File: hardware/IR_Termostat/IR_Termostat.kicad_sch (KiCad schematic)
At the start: 16 parts, among them J1 USB_C_Receptacle_PowerOnly_6P, Q1 PMOS, U1 TP4056-42-ESOP8, U2 XC6206P-3.3V

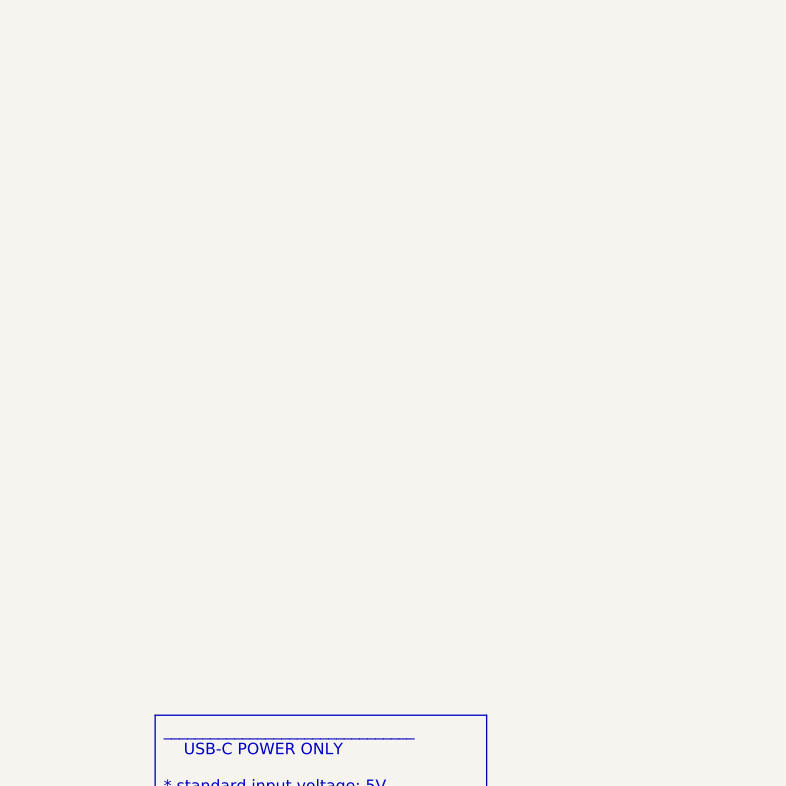
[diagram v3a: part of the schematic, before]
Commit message: feat: Battery protection circuit implemented
Added a protection resiable IC for: Over and Under charge, short, inverse polarity
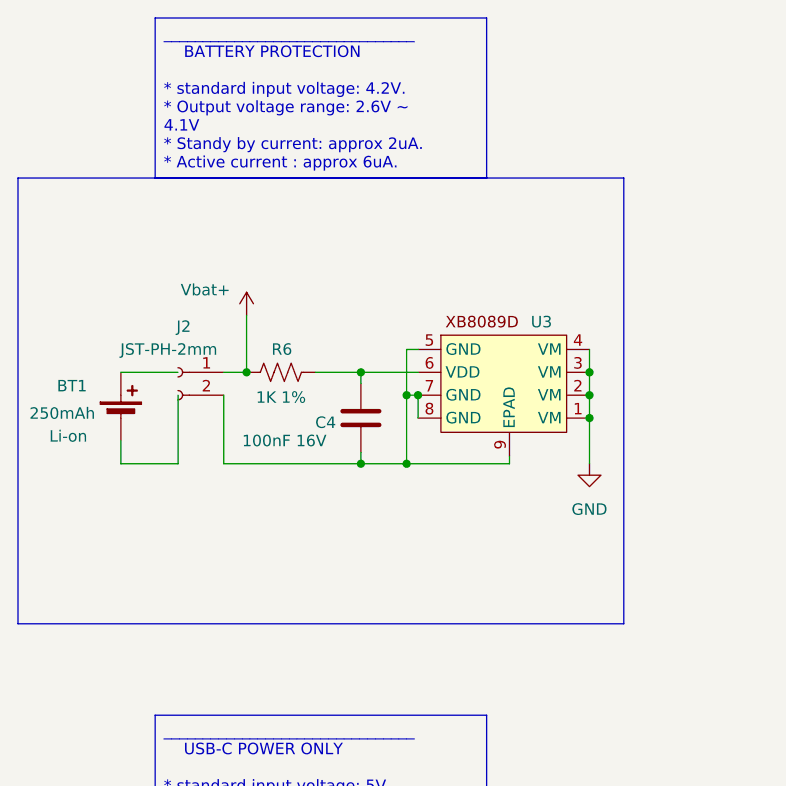
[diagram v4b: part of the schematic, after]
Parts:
- added BT1: 250mAh, symbol Device:Battery_Cell
- added C4: 100nF 16V, Capacitor_SMD:C_0805_2012Metric_Pad1.18x1.45mm_HandSolder, symbol Device:C
- added J2: JST-PH-2mm, Connector_JST:JST_PH_S2B-PH-K_1x02_P2.00mm_Horizontal, symbol Connector:Conn_01x02_Socket
- added R6: 1K 1%, Resistor_SMD:R_0805_2012Metric_Pad1.20x1.40mm_HandSolder, symbol Device:R_US
- added U3: ~, symbol Custom_lib:XB8089D
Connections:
- net GND: now also U3.1 (VM), U3.2 (VM), U3.3 (VM), U3.4 (VM)
- net Vbat+: now also J2.1 (Pin_1), R6.1
- new net: C4.1, R6.2, U3.6 (VDD)
- new net: C4.2, J2.2 (Pin_2), U3.5 (GND), U3.7 (GND), U3.8 (GND), U3.9 (EPAD)

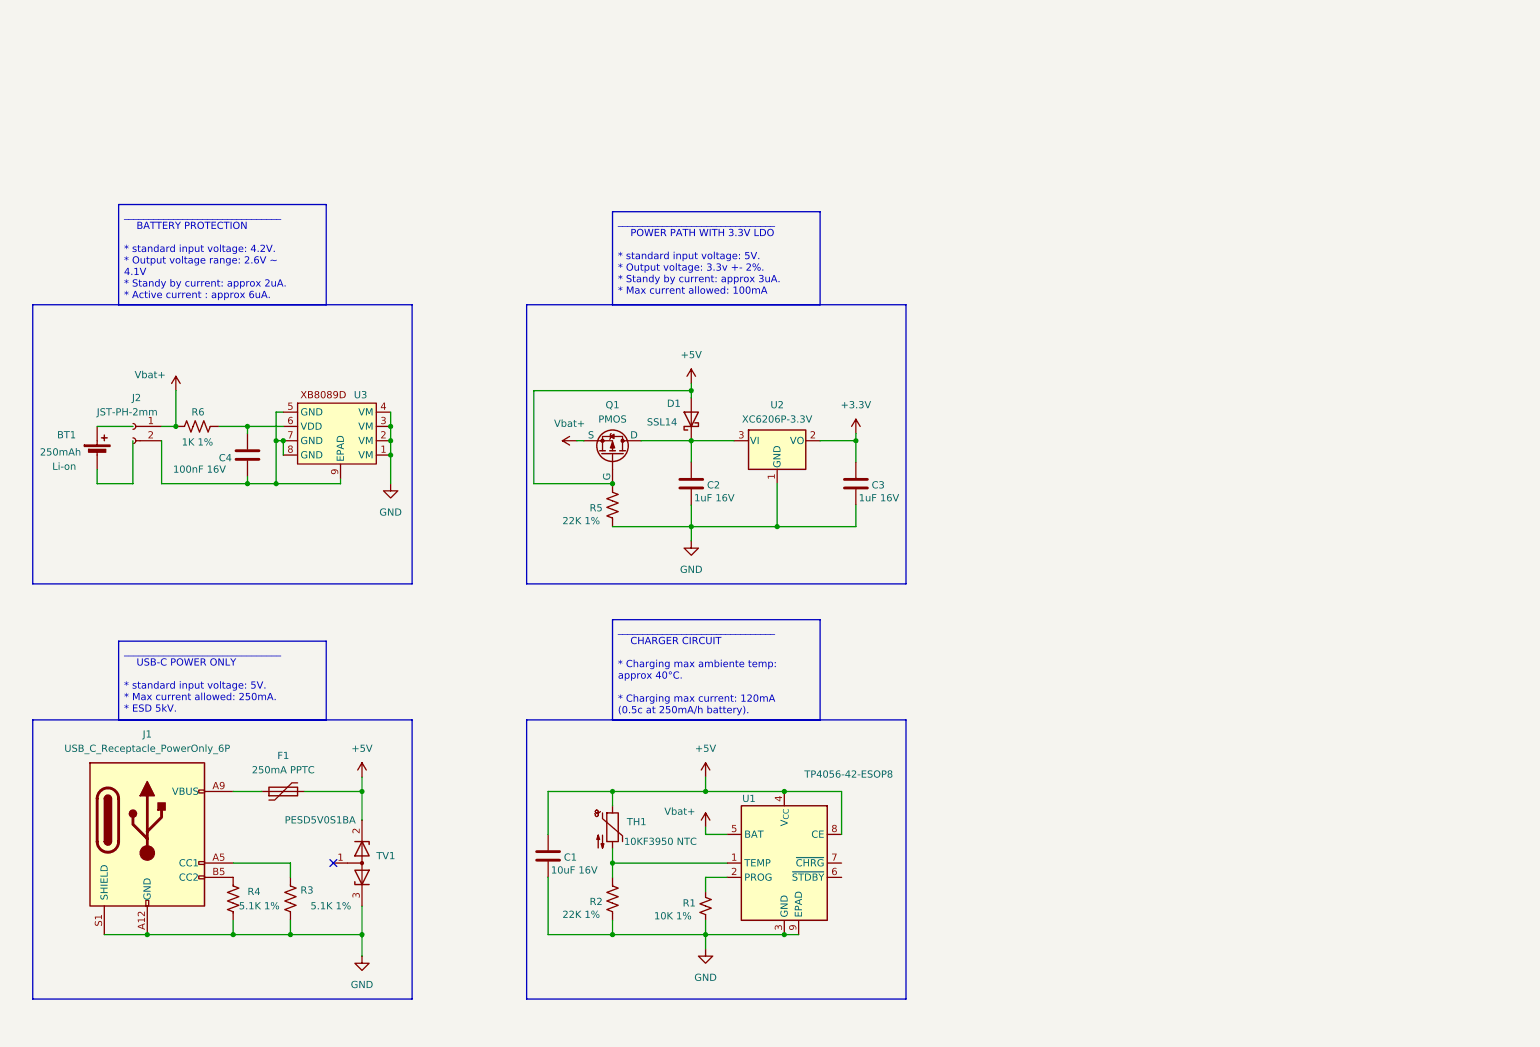
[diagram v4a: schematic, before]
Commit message: feat: pullup resistor to charge IC I/Os
 Also redesingned the sch. for better visual
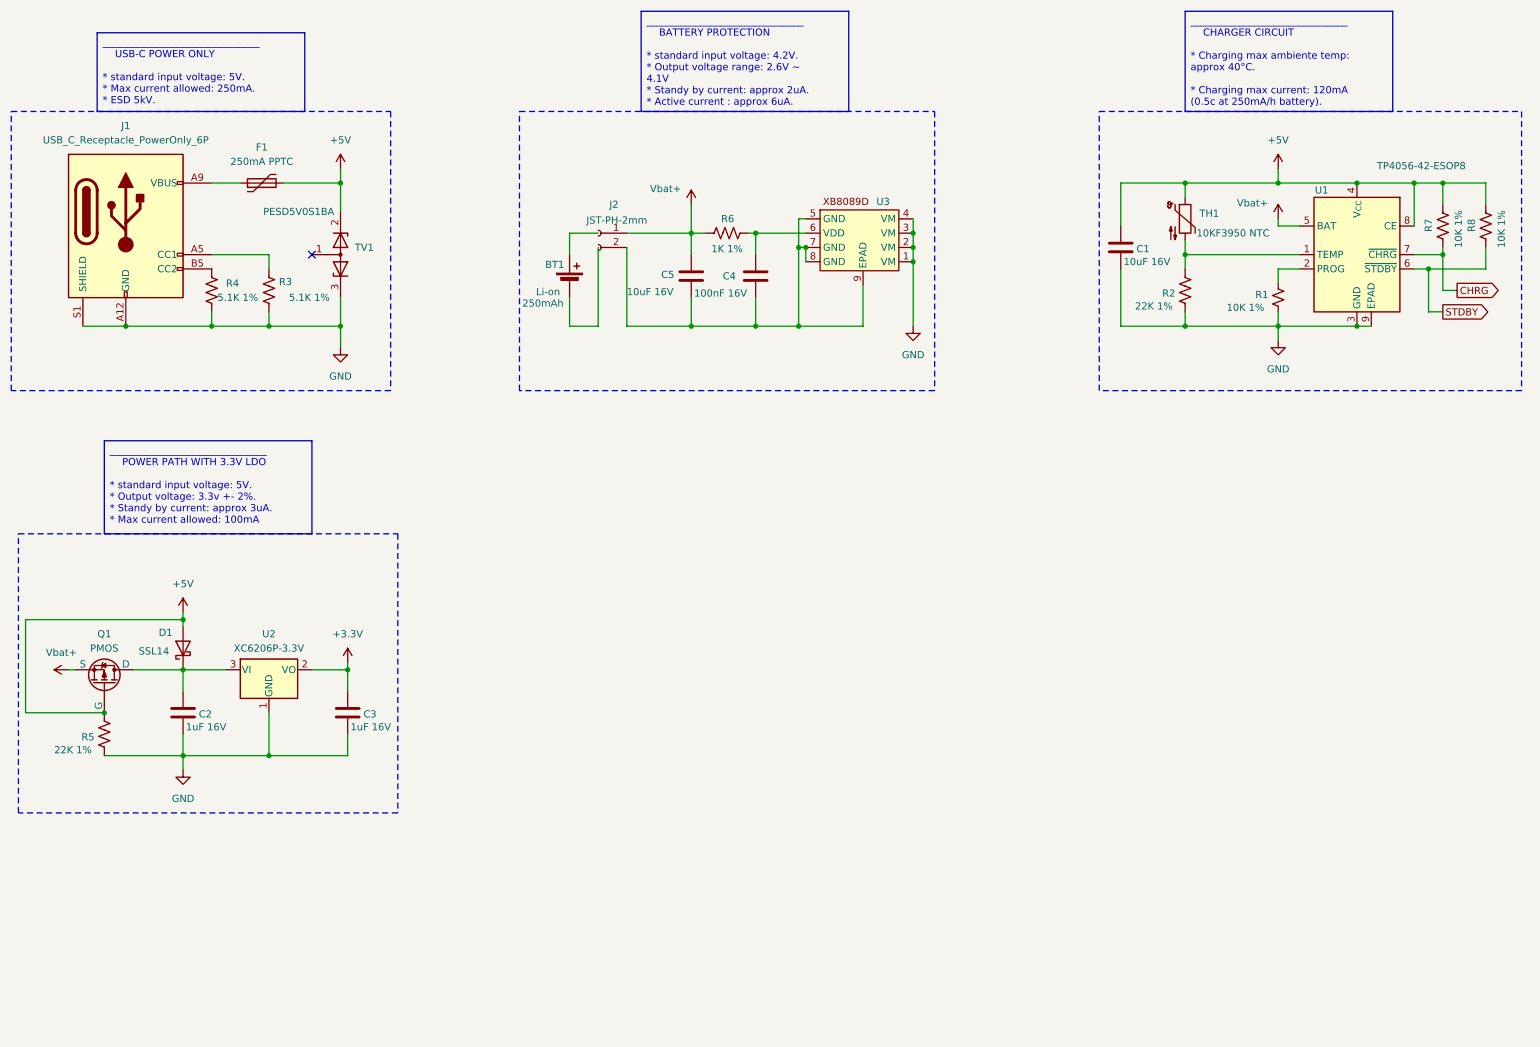
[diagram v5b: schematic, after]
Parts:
- added C5: 10uF 16V, Capacitor_SMD:C_0805_2012Metric_Pad1.18x1.45mm_HandSolder, symbol Device:C
- added R7, R8: 10K 1%, Resistor_SMD:R_0805_2012Metric_Pad1.20x1.40mm_HandSolder, symbol Device:R_US
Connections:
- net +5V: now also R7.2, R8.2
- net Vbat+: now also C5.1
- net at C4.2, J2.2 (Pin_2), U3.5 (GND)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: now also C5.2
- net STDBY: now reaches U1.6 (~{STDBY})
- net STDBY: now also R8.1
- net CHRG: now reaches U1.7 (~{CHRG})
- net CHRG: now also R7.1
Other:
- moved on the sheet: BT1, C1, C2, C3, C4, D1, F1, J1, J2, Q1, R1, R2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

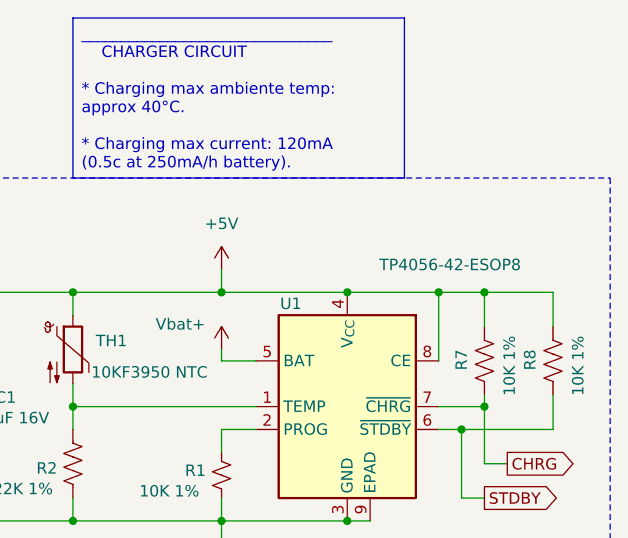
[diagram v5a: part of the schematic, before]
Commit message: Fix: Switched Pullup resistors source from TP4056
Before, the resistors responsable for the pullup of the CHRGD and STDBY pins from the charger IC are connect on 5V line, now they are on 3.3V power supply from LDO.
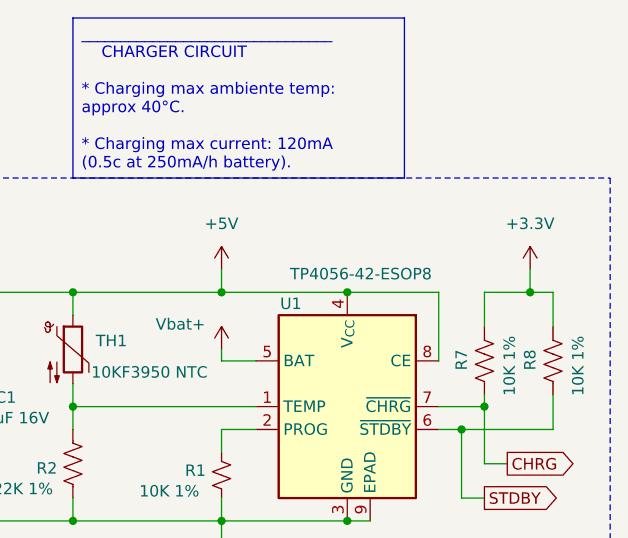
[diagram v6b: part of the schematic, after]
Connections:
- net +3.3V: now also R7.2, R8.2
- net +5V: no longer R7.2, R8.2
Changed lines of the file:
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@@
-	)
-	(junction
-		(at 267.97 44.45)
-		(diameter 0)
-		(color 0 0 0 0)
 	)
 	(junction
@@
 	)
 	(junction
-		(at 262.89 44.45)
-		(diameter 0)
-		(color 0 0 0 0)
-	)
-	(junction
 		(at 44.45 121.92)
 		(diameter 0)
@@
 	)
 	(junction
+		(at 273.05 44.45)
+		(diameter 0)
+		(color 0 0 0 0)
+	)
+	(junction
 		(at 173.99 55.88)
 		(diameter 0)
@@
 	(wire
 		(pts
+			(xy 273.05 44.45) (xy 275.59 44.45)
+		)
+		(stroke
+			(width 0)
+			(type default)
+		)
+	)
+	(wire
+		(pts
 			(xy 134.62 57.15) (xy 134.62 53.34)
 		)
@@
 	(wire
 		(pts
+			(xy 273.05 41.91) (xy 273.05 44.45)
+		)
+		(stroke
+			(width 0)
+			(type default)
+		)
+	)
+	(wire
+		(pts
 			(xy 238.76 44.45) (xy 252.73 44.45)
 		)
@@
 	(wire
 		(pts
-			(xy 267.97 44.45) (xy 275.59 44.45)
+			(xy 267.97 44.45) (xy 273.05 44.45)
 		)
 		(stroke
@@
 		(pts
 			(xy 222.25 69.85) (xy 238.76 69.85)
-		)
-		(stroke
-			(width 0)
-			(type default)
-		)
-	)
-	(wire
-		(pts
-			(xy 262.89 44.45) (xy 267.97 44.45)
 		)
 		(stroke
@@
 		)
 		(property "Value" "TP4056-42-ESOP8"
-			(at 272.034 41.402 0)
+			(at 262.128 42.418 0)
 			(effects
 				(font
@@
 					(unit 1)
 				)
+			)
+		)
+	)
+	(symbol
+		(lib_id "power:+3.3V")
+		(at 273.05 41.91 0)
+		(unit 1)
+		(exclude_from_sim no)
+		(in_bom yes)
+		(on_board yes)
+		(dnp no)
+		(fields_autoplaced yes)
+		(property "Reference" "#PWR015"
+			(at 273.05 45.72 0)
+			(effects
+				(font
+					(size 1.27 1.27)
+				)
+				(hide yes)
+			)
+		)
+		(property "Value" "+3.3V"
+			(at 273.05 36.83 0)
+			(effects
+				(font
+					(size 1.27 1.27)
+				)
+			)
+		)
+		(property "Footprint" ""
+			(at 273.05 41.91 0)
+			(effects
+				(font
+					(size 1.27 1.27)
+				)
+				(hide yes)
+			)
+		)
+		(property "Datasheet" ""
+			(at 273.05 41.91 0)
+			(effects
+				(font
+					(size 1.27 1.27)
+				)
+				(hide yes)
+			)
+		)
+		(property "Description" "Power symbol creates a global label with name \"+3.3V\""
+			(at 273.05 41.91 0)
+			(effects
+				(font
+					(size 1.27 1.27)
+				)
+				(hide yes)
+			)
+		)
+		(pin "1"
+		)
+		(instances
+			(project "IR_Termostat"
+				(path "/2f75bfd1-14b3-4bd7-8351-dce181eee92d"
+					(reference "#PWR015")
+					(unit 1)
+				)

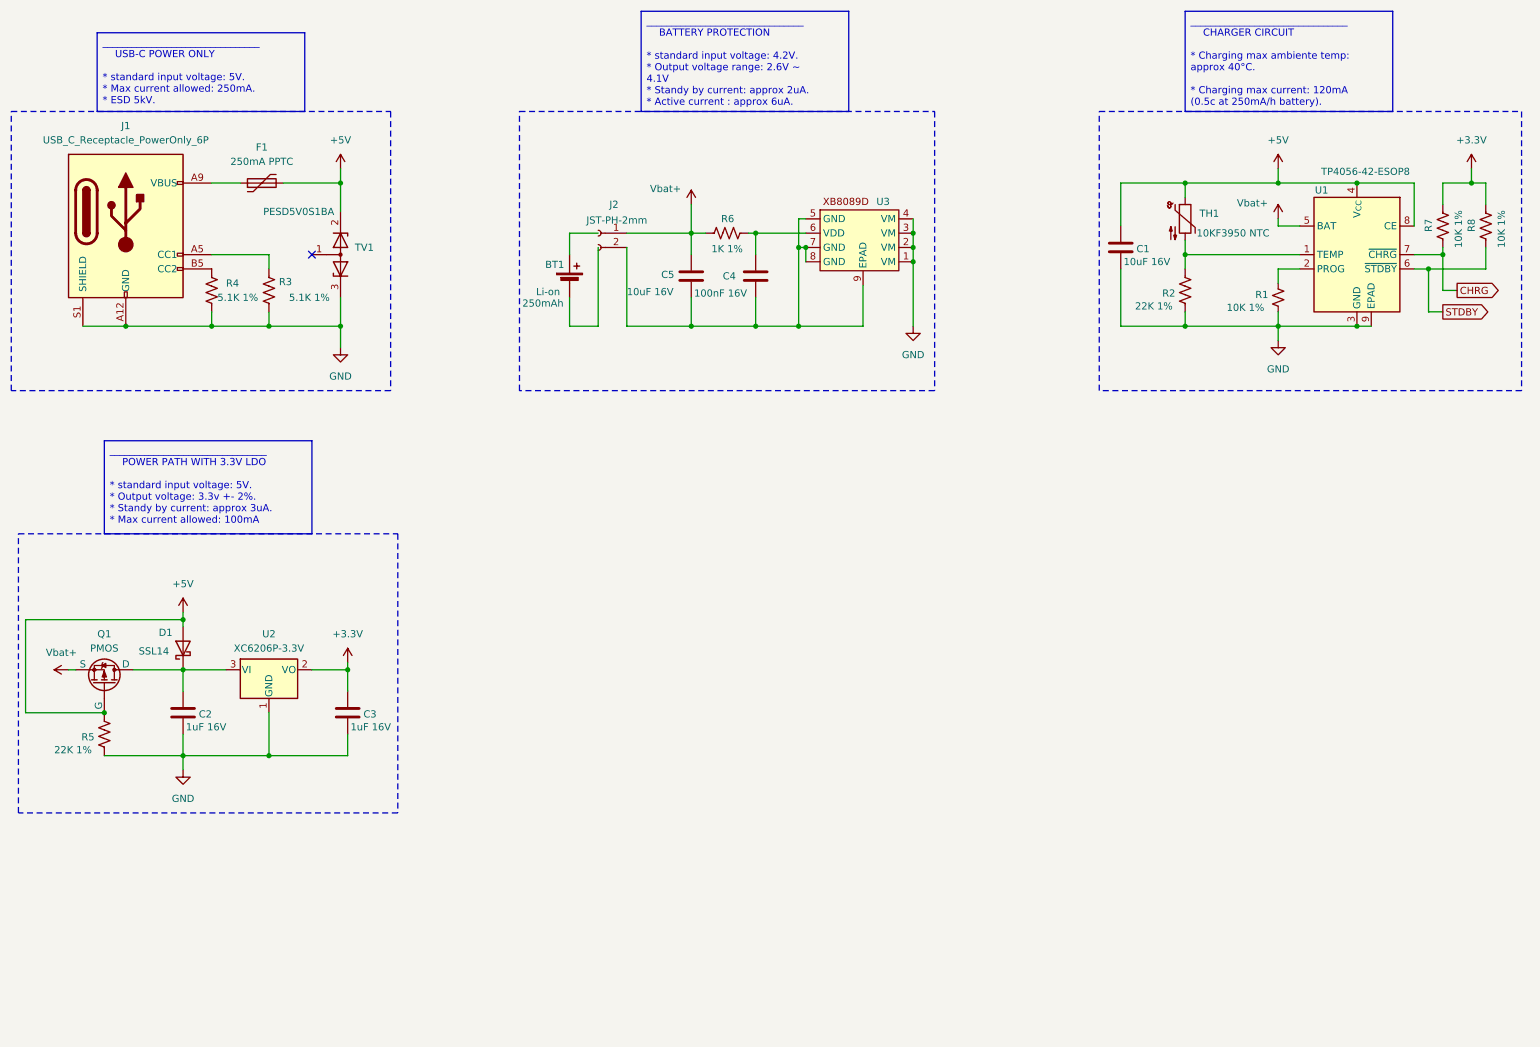
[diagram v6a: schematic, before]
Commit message: Feat: main MCU and ADC
Included the CH32V003J4M6, also bring up a voltage divider with overrange protection to read the battery voltage with realible, and brightness mensurement with another ADC channel.
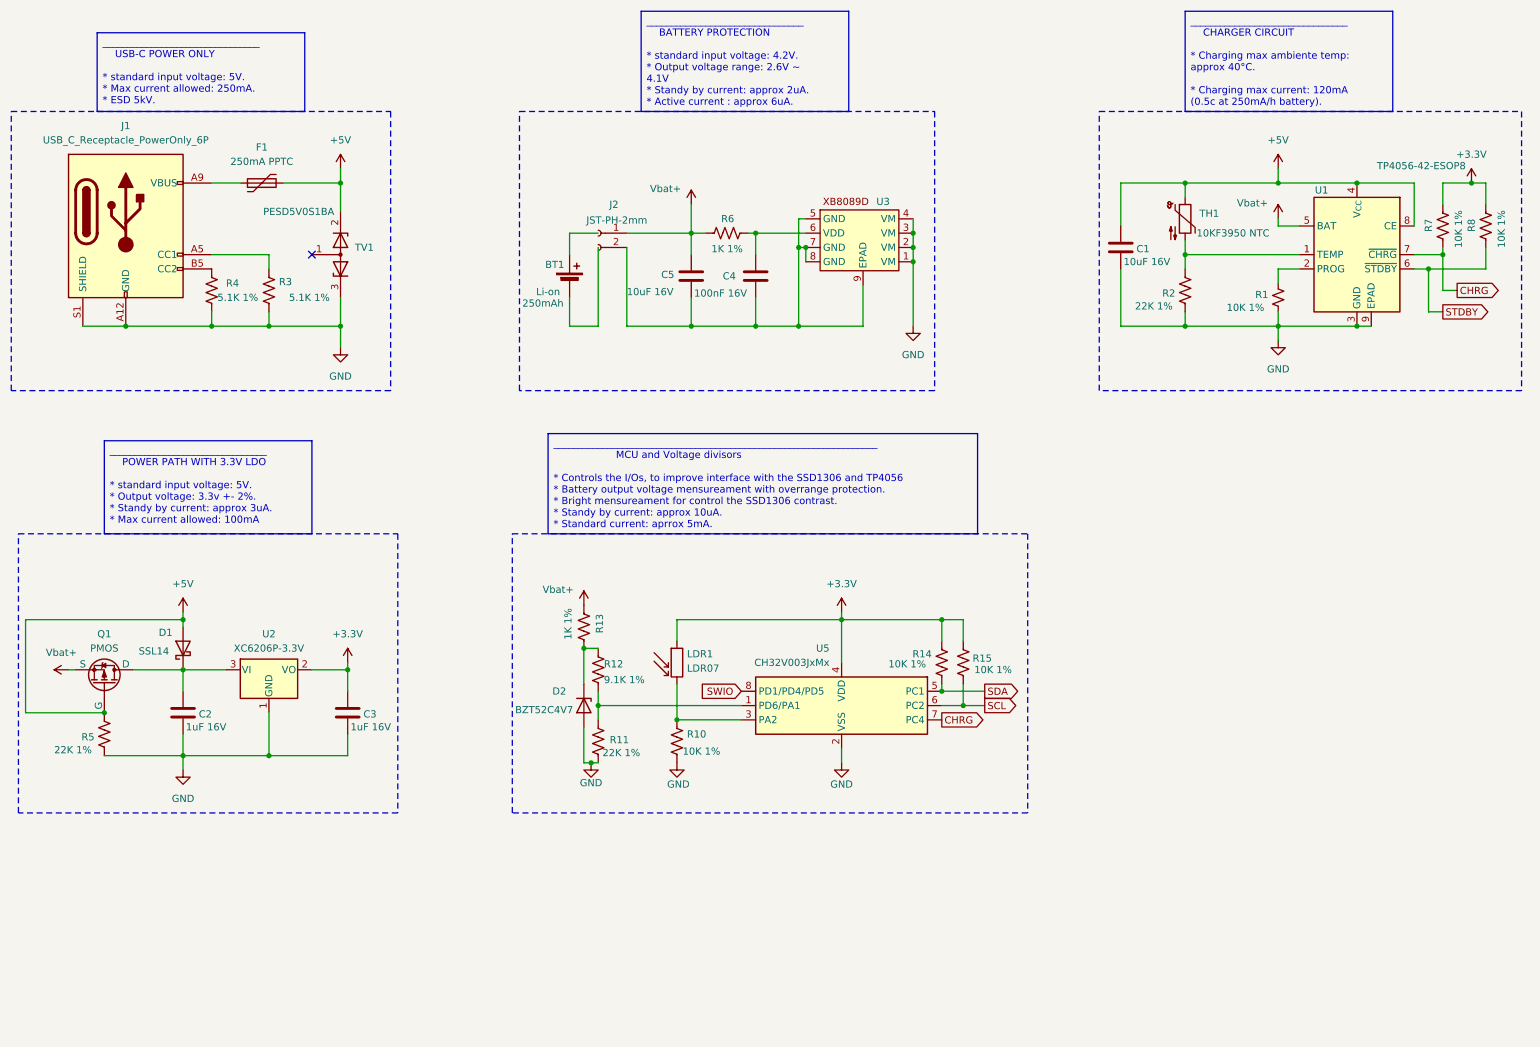
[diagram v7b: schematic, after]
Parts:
- added D2: BZT52C4V7, Diode_SMD:D_SOD-123F, symbol Diode:BZT52Bxx
- added LDR1: LDR07, OptoDevice:R_LDR_5.1x4.3mm_P3.4mm_Vertical, symbol Sensor_Optical:LDR07
- added R10, R14, R15: 10K 1%, Resistor_SMD:R_0805_2012Metric_Pad1.20x1.40mm_HandSolder, symbol Device:R_US
- added R11: 22K 1%, Resistor_SMD:R_0805_2012Metric_Pad1.20x1.40mm_HandSolder, symbol Device:R_US
- added R12: 9.1K 1%, Resistor_SMD:R_0805_2012Metric_Pad1.20x1.40mm_HandSolder, symbol Device:R_US
- added R13: 1K 1%, Resistor_SMD:R_0805_2012Metric_Pad1.20x1.40mm_HandSolder, symbol Device:R_US
- added U5: CH32V003JxMx, Package_SO:SOP-8_3.9x4.9mm_P1.27mm, symbol MCU_WCH_CH32V0:CH32V003JxMx
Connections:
- net +3.3V: now also LDR1.1, R14.2, R15.2, U5.4 (VDD)
- net CHRG: now also U5.7 (PC4)
- net GND: now also D2.2 (A), R10.2, R11.2, U5.2 (VSS)
- net Vbat+: now also R13.2
- new net: D2.1 (K), R12.1, R13.1
- new net: LDR1.2, R10.1, U5.3 (PA2)
- new net: R11.1, R12.2, U5.1 (PD6/PA1)
- new net SCL: R15.1, U5.6 (PC2)
- new net SDA: R14.1, U5.5 (PC1)
- new net SWIO: U5.8 (PD1/PD4/PD5)
